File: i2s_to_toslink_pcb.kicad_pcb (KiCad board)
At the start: 2 copper layers, 61.9 x 63.1 mm, 71 parts, among them J1 FTDI_6P, J10 FCR684204T, J11 DIN_DOUT_2TP, J12 MCU_GPIOS, J13 AJ_TP5, J14 C_G0, J15 C_G7, J16 CRST, J17 C_CLKOUT, J2 EXT_CLK_IN5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

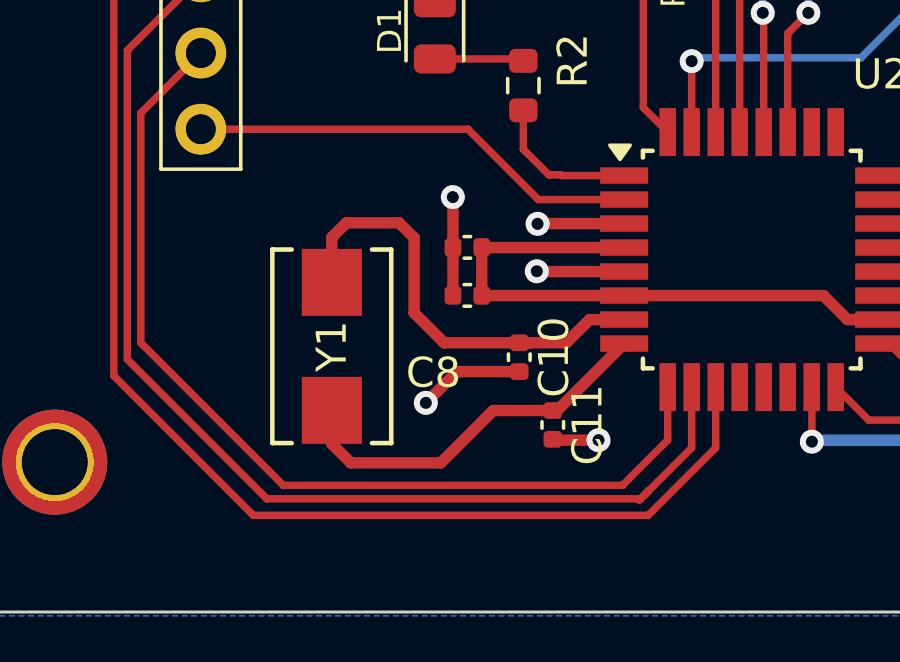
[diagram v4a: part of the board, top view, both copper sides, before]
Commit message: 16M mcu crystal changed to 12M
- Atmel168A crystal max frequency can be about
  13.3 Mhz for 3V3 voltage.
  See atmega168a datasheet Figure 29-1. Maximum Frequency vs. VCC
--> 10MHz + 10Mhz/(4.5 - 2.7) * (3.3 - 2.7) = 13.3Mhz

Signed-off-by: Mika Laitio <lamikr@gmail.com>
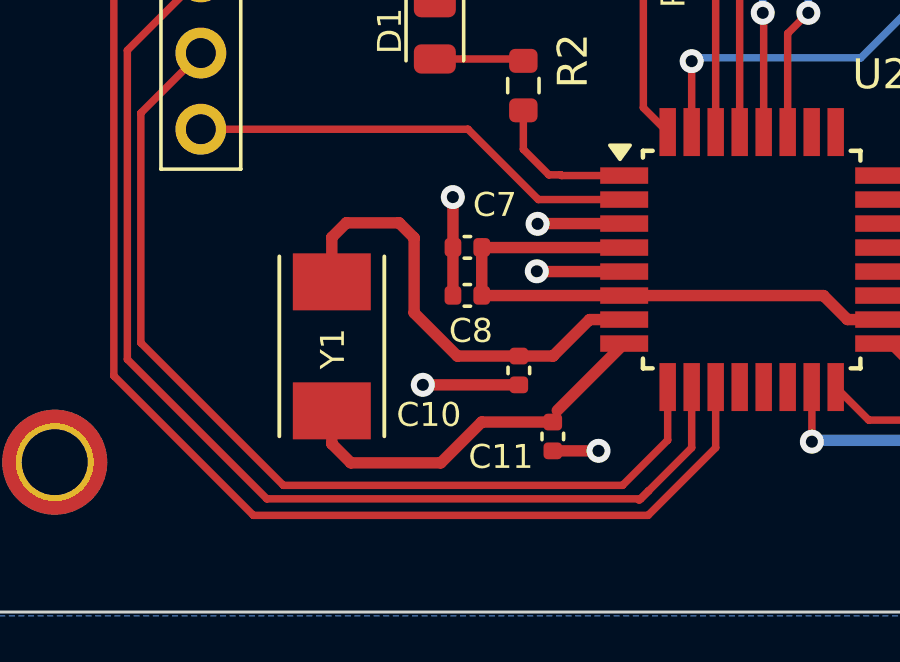
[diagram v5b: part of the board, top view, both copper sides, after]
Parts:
- Y1: value 16M -> 12M; footprint lamikr_audio:XTAL_ABM7_ABR -> lamikr_audio:XTAL_ABM7-12.000MHZ-D2Y-T
- moved C10 0.44 mm to (39.6, 74.9)
- moved C11 0.38 mm to (40.7, 77.1)

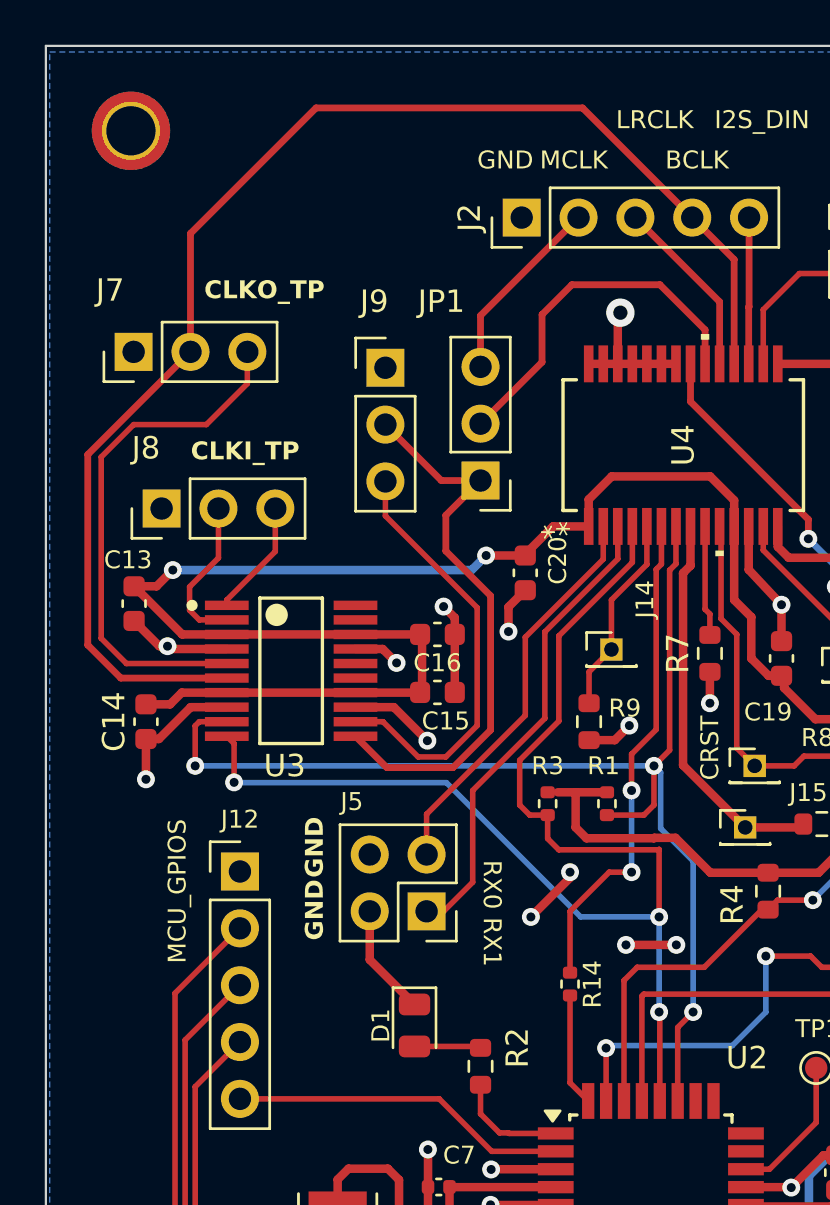
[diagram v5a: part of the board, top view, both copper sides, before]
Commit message: add pull-up resistors for codex rx-pins
- add connectors for rx0 and rx1 pins
- rest of the rx-pins not reserved for use
  and they will share a common pull-up.

Signed-off-by: Mika Laitio <lamikr@gmail.com>
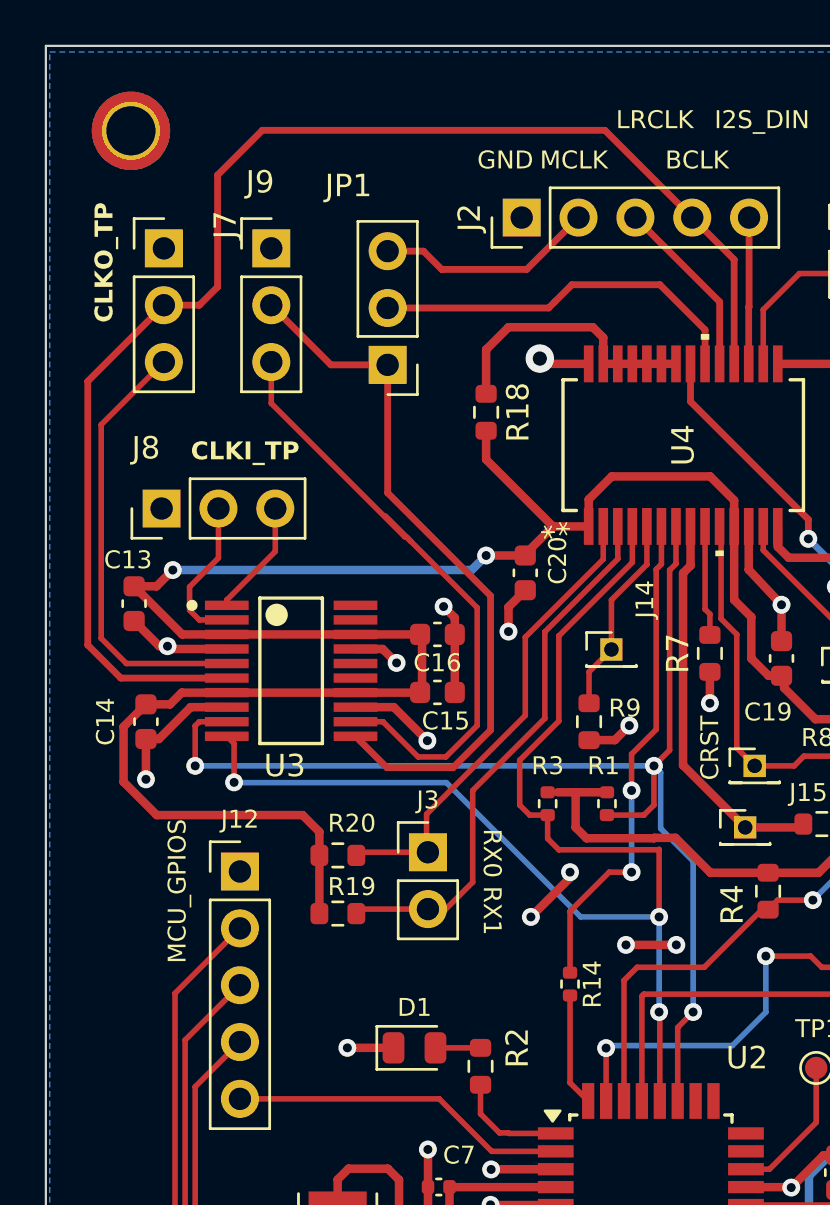
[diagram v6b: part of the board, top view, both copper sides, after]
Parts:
- removed J5: RX0/RX1, Connector_PinHeader_2.54mm:PinHeader_2x02_P2.54mm_Vertical
- added J3: Conn_01x02_Pin, Connector_PinHeader_2.54mm:PinHeader_1x02_P2.54mm_Vertical, F.Cu at (37.4, 55.9)
- added R18: 10k, Resistor_SMD:R_0603_1608Metric, F.Cu at (40.0, 36.2)
- added R19: 3k, Resistor_SMD:R_0603_1608Metric, F.Cu at (33.4, 58.6)
- added R20: 3k, Resistor_SMD:R_0603_1608Metric, F.Cu at (33.4, 56.0)
- moved J9 7.38 mm to (30.4, 28.9)
- moved JP1 6.63 mm to (35.6, 34.1)
- moved J7 4.82 mm to (25.6, 28.9), turned to 0 degrees
- moved D1 1.00 mm to (36.8, 64.6), turned to 0 degrees
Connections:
- U4 pad 22: GND -> Net-(U4-RX2)
- U4 pad 23: GND -> Net-(U4-RX2)
- U4 pad 24: GND -> Net-(U4-RX2)
- U4 pad 25: GND -> Net-(U4-RX2)
- U4 pad 26: GND -> Net-(U4-RX2)
- U4 pad 27: GND -> Net-(U4-RX2)
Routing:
- net VCC_3V3: track 213.2 -> 235.9 mm
- net Net-(U4-RX2): track 0.00 -> 12.2 mm
- net Net-(J9-Pin_3): track 19.3 -> 28.4 mm
- net GND: track 122.7 -> 115.8 mm, vias 30 -> 31
- net CLKGEN_OUT_I2S_MCLK: track 25.2 -> 31.8 mm
- net Net-(J7-Pin_3): track 23.5 -> 19.6 mm
- net Net-(J3-Pin_2): track 21.2 -> 24.5 mm
- net Net-(J3-Pin_1): track 17.9 -> 21.2 mm
- net EXTERNAL_IN_I2S_MCLK: track 8.48 -> 9.83 mm
- net EXTERNAL_IN_I2S_BCLK: track 61.2 -> 62.1 mm
- net Net-(D1-A): track 2.89 -> 2.01 mm
- net CODEC_IN_I2S_MCLK: track 16.2 -> 17.0 mm

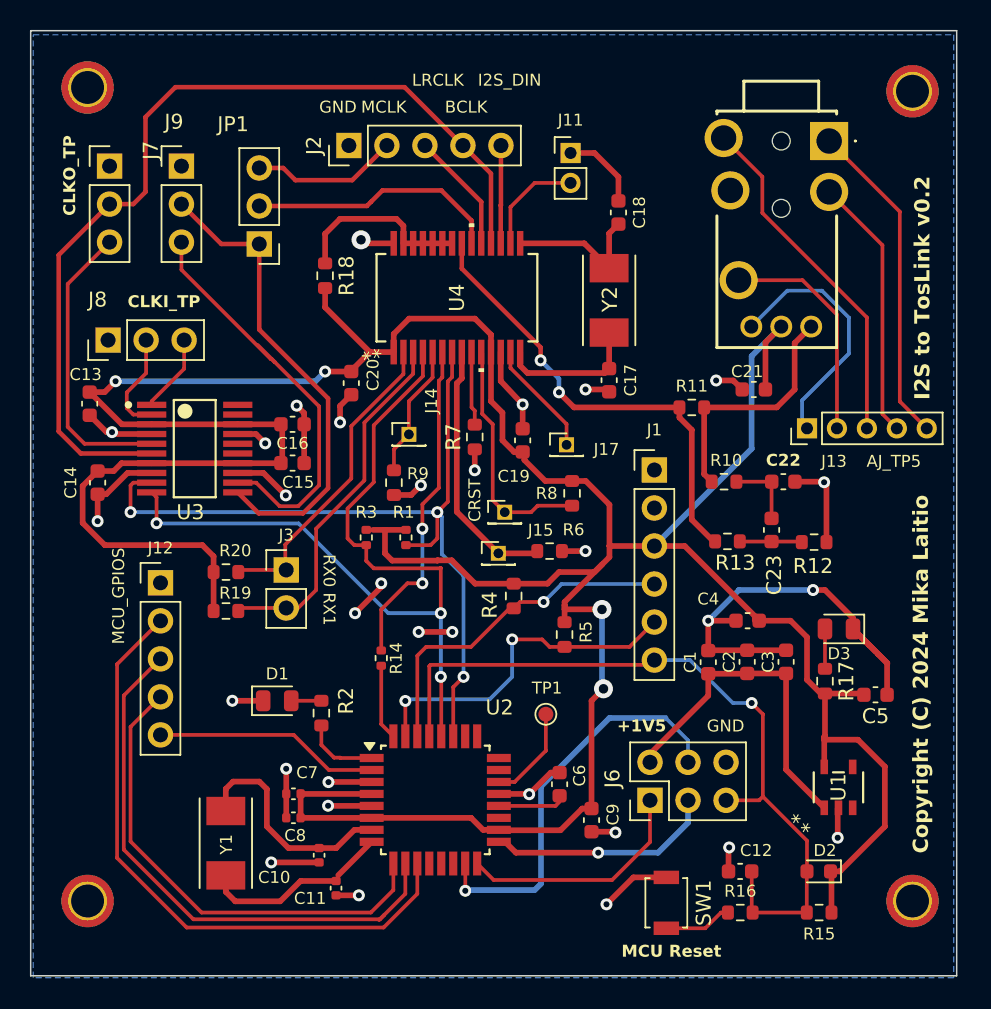
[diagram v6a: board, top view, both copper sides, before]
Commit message: rework the atmega168 reset signal schematics and routing
Signed-off-by: Mika Laitio <lamikr@gmail.com>
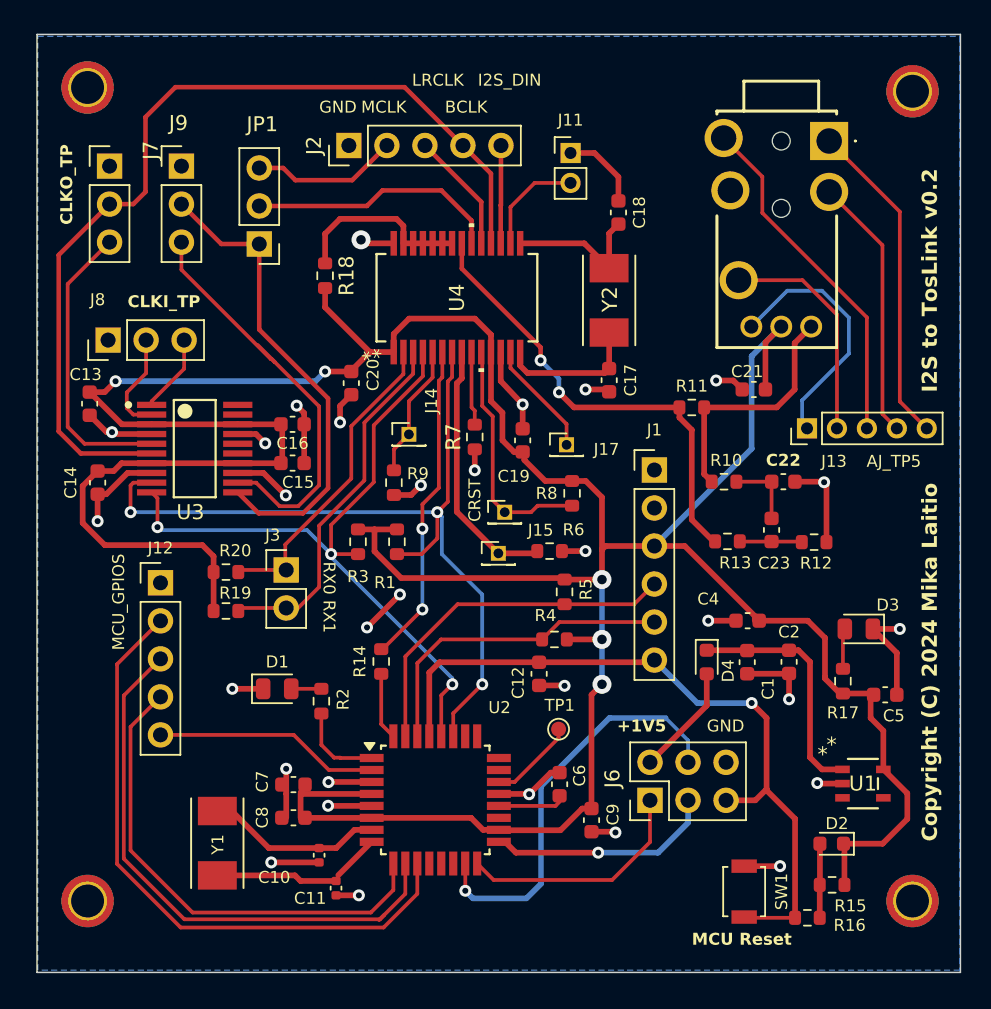
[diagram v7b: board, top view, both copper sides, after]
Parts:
- removed C3: 1uF, Capacitor_SMD:C_0603_1608Metric
- added D4: D_Schottky, Diode_SMD:D_0603_1608Metric, F.Cu at (65.5, 62.0)
- C12: value 100nF -> 0u1F
- C7, C8: footprint Capacitor_SMD:C_0402_1005Metric -> Capacitor_SMD:C_0603_1608Metric
- R1, R14, R3: footprint Resistor_SMD:R_0402_1005Metric -> Resistor_SMD:R_0603_1608Metric
- R15: value 4k7 -> 10k
- moved C12 18.8 mm to (54.3, 62.8), turned to -90 degrees
- moved SW1 5.25 mm to (68.0, 77.3)
- moved R16 4.50 mm to (72.2, 79.1)
- moved R4 3.98 mm to (55.3, 60.5), turned to 0 degrees
- moved R5 2.85 mm to (56.0, 57.3)
- moved C2 2.80 mm to (71.0, 62.0), turned to -90 degrees
- moved C1 2.60 mm to (68.2, 62.0), turned to -90 degrees
- moved D2 2.04 mm to (73.8, 74.2)
- moved R15 2.04 mm to (73.9, 76.9)
- moved U1 1.65 mm to (75.9, 70.1), turned to 0 degrees
- moved D3 1.32 mm to (75.7, 59.8)
- moved TP1 1.31 mm to (55.6, 66.5)
- moved R17 1.20 mm to (74.6, 63.3)
- moved D1 0.80 mm to (36.8, 63.8)
- moved R2 0.80 mm to (39.8, 64.6)
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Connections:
- C1 pad 1: VIN_5V -> Net-(D4-K)
- C2 pad 1: VIN_5V -> Net-(D4-K)
- D2 pad 2: MCU_RST -> Net-(D2-A)
- J1 pad 4: MCU_RXD0 -> MCU_TXD0
- J1 pad 5: MCU_TXD0 -> MCU_RXD0
- R15 pad 2: MCU_RST -> Net-(D2-A)
- R16 pad 1: Net-(R16-Pad1) -> MCU_RST
- R16 pad 2: MCU_RST -> Net-(D2-A)
- SW1 pad 2: Net-(R16-Pad1) -> MCU_RST
- U1 pad 1: VIN_5V -> Net-(D4-K)
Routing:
- net GND: track 115.8 -> 95.2 mm, vias 31 -> 30
- net Net-(D4-K): track 0.00 -> 15.8 mm
- net VIN_5V: track 22.2 -> 7.48 mm
- net MCU_SCL1: track 57.2 -> 48.5 mm
- net VCC_3V3: track 235.9 -> 230.3 mm, vias 4 -> 5
- net Net-(D2-A): track 0.00 -> 4.89 mm
- net Net-(R16-Pad1): track 4.55 -> 0.00 mm
- net MCU_XTAL1: track 15.3 -> 10.9 mm
- net MCU_RST: track 51.5 -> 49.1 mm
- net MCU_SDA1: track 54.9 -> 56.8 mm
- net MCU_XTAL2: track 12.5 -> 11.2 mm
- net MCU_RXD0: track 22.9 -> 21.9 mm, vias 1 -> 0
- net Net-(J3-Pin_2): track 24.5 -> 23.4 mm
- net MCU_TXD0: track 23.1 -> 24.0 mm, vias 2 -> 0
- net MCU_LED: track 5.02 -> 5.82 mm
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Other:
- board size 61.9 x 63.1 mm -> 61.7 x 62.7 mm

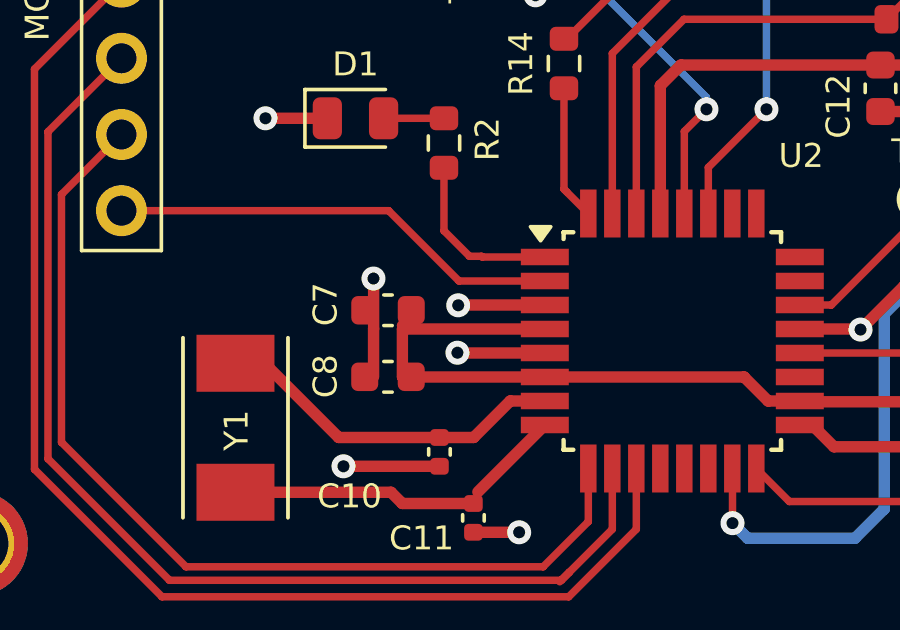
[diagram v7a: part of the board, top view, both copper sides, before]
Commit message: cleaned routing on C7 and C8 area
Signed-off-by: Mika Laitio <lamikr@gmail.com>
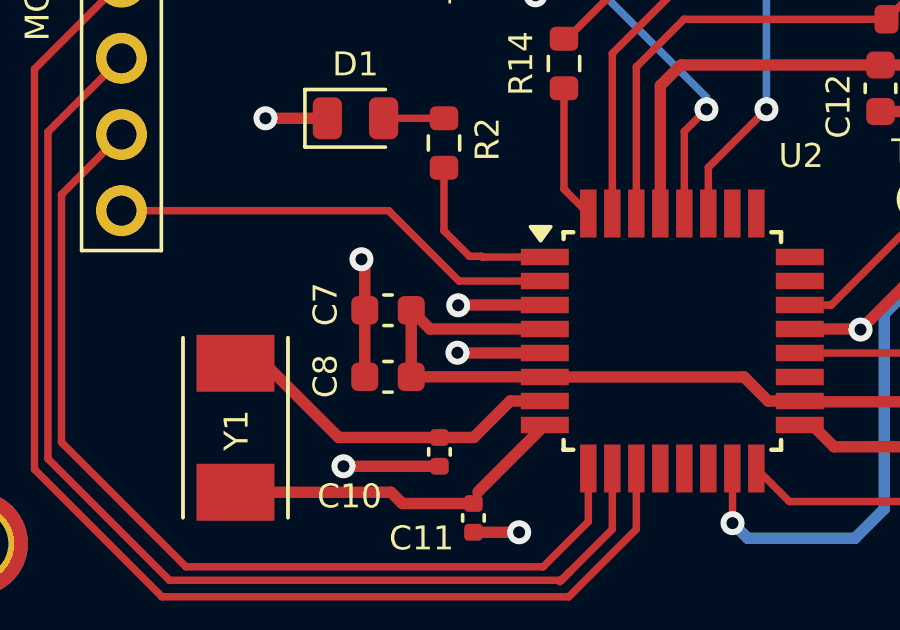
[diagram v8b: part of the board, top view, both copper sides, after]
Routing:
- net GND: track 95.2 -> 95.7 mm
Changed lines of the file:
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@@
-	)
-	(segment
-		(start 37.4046 70.8178)
-		(end 37.4046 69.146)
-		(width 0.381)
-		(layer "F.Cu")
-		(net 1)
 	)
 	(segment
@@
 	)
 	(segment
+		(start 37.1086 70.201)
+		(end 37.1096 70.2)
+		(width 0.381)
+		(layer "F.Cu")
+		(net 1)
+	)
+	(segment
+		(start 37.1096 70.2)
+		(end 37.1096 68.6096)
+		(width 0.381)
+		(layer "F.Cu")
+		(net 1)
+	)
+	(segment
 		(start 67.2725 43.2)
 		(end 67.8725 43.8)
@@
 	)
 	(segment
+		(start 37.1096 68.6096)
+		(end 37 68.5)
+		(width 0.381)
+		(layer "F.Cu")
+		(net 1)
+	)
+	(segment
 		(start 67.455 59.25)
 		(end 65.6 59.25)
@@
 	)
 	(segment
-		(start 37.4036 72.418)
-		(end 37.4036 70.8188)
-		(width 0.381)
-		(layer "F.Cu")
-		(net 1)
-	)
-	(segment
 		(start 59.6 29.6)
 		(end 58 28)
@@
 	)
 	(segment
-		(start 37.4046 69.146)
-		(end 37.4 69.1414)
-		(width 0.381)
-		(layer "F.Cu")
-		(net 1)
-	)
-	(segment
 		(start 71.3924 49.9614)
 		(end 73.3042 49.9614)
@@
 	)
 	(segment
+		(start 37.1086 72.418)
+		(end 37.1086 70.201)
+		(width 0.381)
+		(layer "F.Cu")
+		(net 1)
+	)
+	(segment
 		(start 58 28)
 		(end 56.4 28)
@@
 		(start 43.1114 70.0242)
 		(end 40.2335 70.0242)
-		(width 0.381)
-		(layer "F.Cu")
-		(net 1)
-	)
-	(segment
-		(start 37.4046 69.2684)
-		(end 37.2776 69.1414)
 		(width 0.381)
 		(layer "F.Cu")
@@
 	)
 	(via
-		(at 37.4 69.1414)
+		(at 37 68.5)
 		(size 0.8)
 		(drill 0.4)
@@
 	)
 	(segment
-		(start 38.4742 70.818)
-		(end 38.3662 70.71)
-		(width 0.381)
-		(layer "F.Cu")
-		(net 49)
-	)
-	(segment
 		(start 78.9 72.5)
 		(end 78.9 70.784748)
@@
 	)
 	(segment
-		(start 43.1114 72.4242)
-		(end 38.3698 72.4242)
+		(start 38.6586 72.418)
+		(end 38.6586 70.201)
 		(width 0.381)
 		(layer "F.Cu")
@@
 	)
 	(segment
-		(start 43.1114 70.8242)
-		(end 38.371 70.8242)
-		(width 0.381)
-		(layer "F.Cu")
-		(net 49)
-	)
-	(segment
 		(start 73.4 63.115)
 		(end 73.4 63)
@@
 	)
 	(segment
+		(start 38.6586 72.418)
+		(end 43.1052 72.418)
+		(width 0.381)
+		(layer "F.Cu")
+		(net 49)
+	)
+	(segment
 		(start 72.25 59.25)
 		(end 69.005 59.25)
@@
 	)
 	(segment
-		(start 38.3636 72.418)
-		(end 38.3636 70.8188)
-		(width 0.381)
-		(layer "F.Cu")
-		(net 49)
-	)
-	(segment
 		(start 50.0126 39.0652)
 		(end 51.084 40.1366)
@@
 	)
 	(segment
+		(start 43.1052 72.418)
+		(end 43.1114 72.4242)
+		(width 0.381)
+		(layer "F.Cu")
+		(net 49)
+	)
+	(segment
 		(start 43.3 53.15)
 		(end 44.8 53.15)
@@
 	)
 	(segment
+		(start 43.1114 70.8242)
+		(end 39.2838 70.8242)
+		(width 0.381)
+		(layer "F.Cu")
+		(net 49)
+	)
+	(segment
 		(start 44.584001 41.3004)
 		(end 44.584001 40.0939)
@@
 	)
 	(segment
+		(start 39.2838 70.8242)
+		(end 38.6596 70.2)
+		(width 0.381)
+		(layer "F.Cu")
+		(net 49)
+	)
+	(segment
 		(start 74.6 64.115)
 		(end 76.565 64.115)
@@
 		(width 0.381)
 		(layer "F.Cu")
+		(net 49)
+	)
+	(segment
+		(start 38.6586 70.201)
+		(end 38.6596 70.2)
+		(width 0.381)
+		(layer "F.Cu")
